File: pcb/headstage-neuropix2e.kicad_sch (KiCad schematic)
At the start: 7 parts, among them J1 X.FL-R-SMT-1(02)

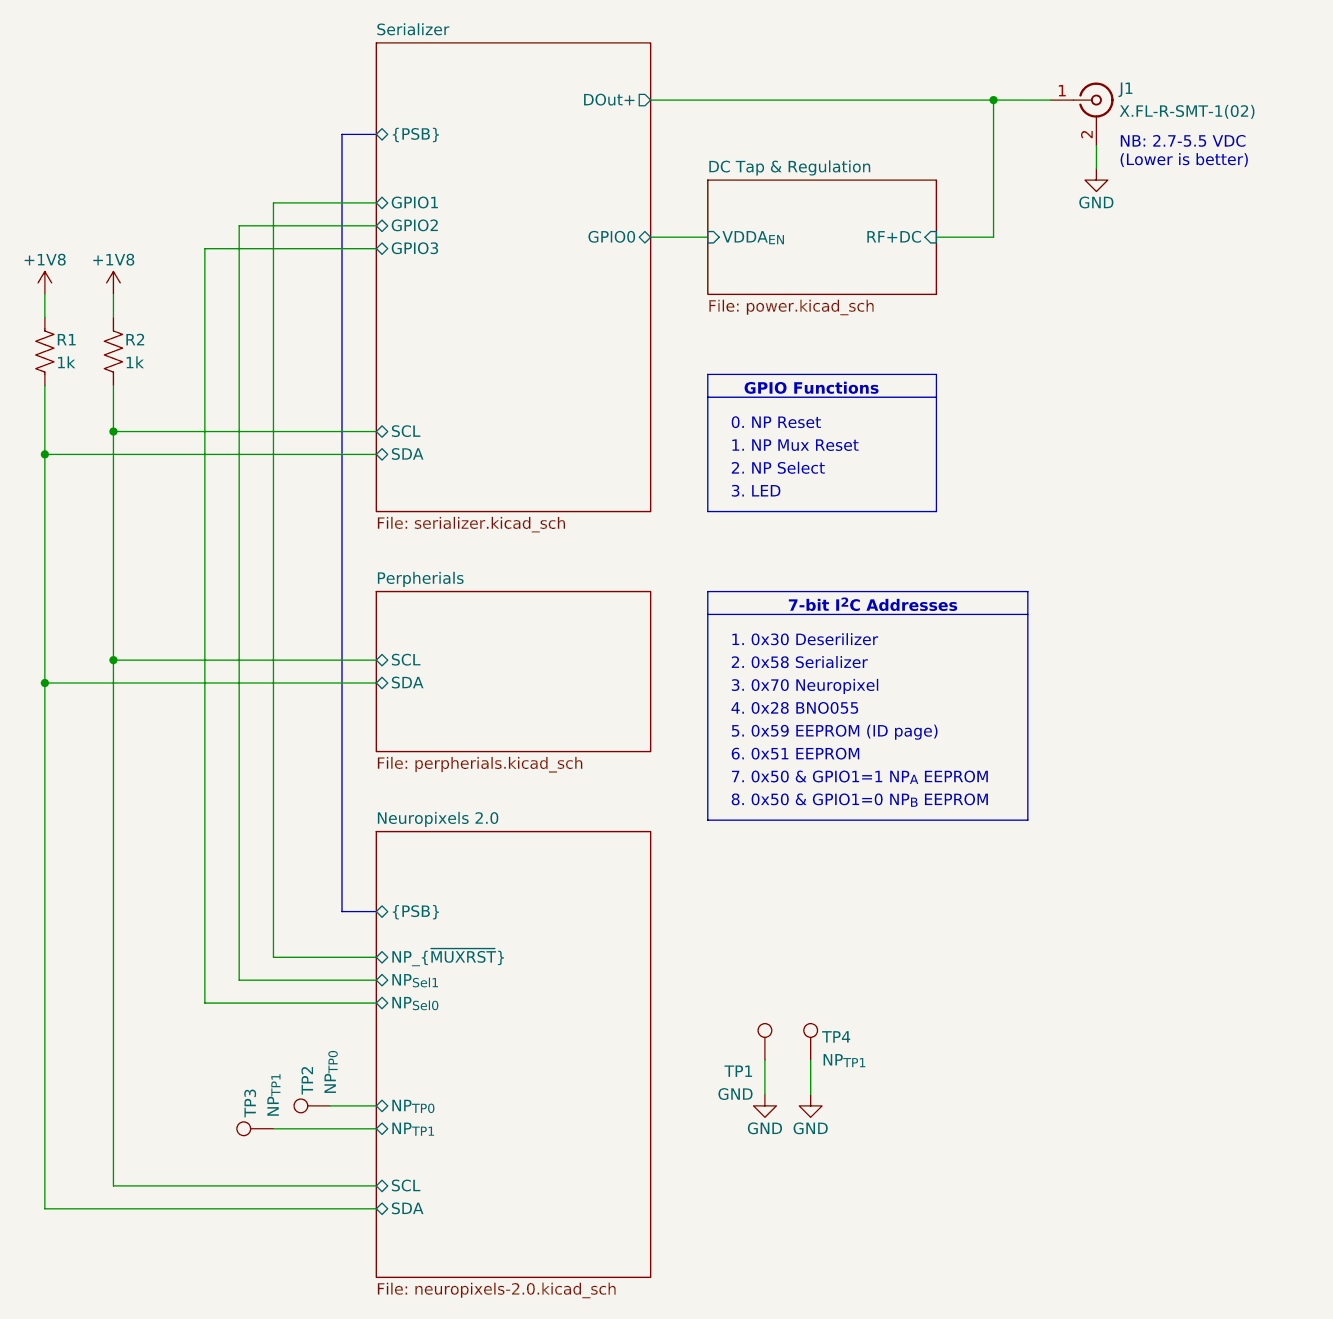
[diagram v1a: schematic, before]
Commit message: Revision B
- Fix incorrect STG3856 symbol and make corresponding changes to PCB
- Flip bits 1 and 2 in probe interaces (fixes #1)
- Improve silkscreen
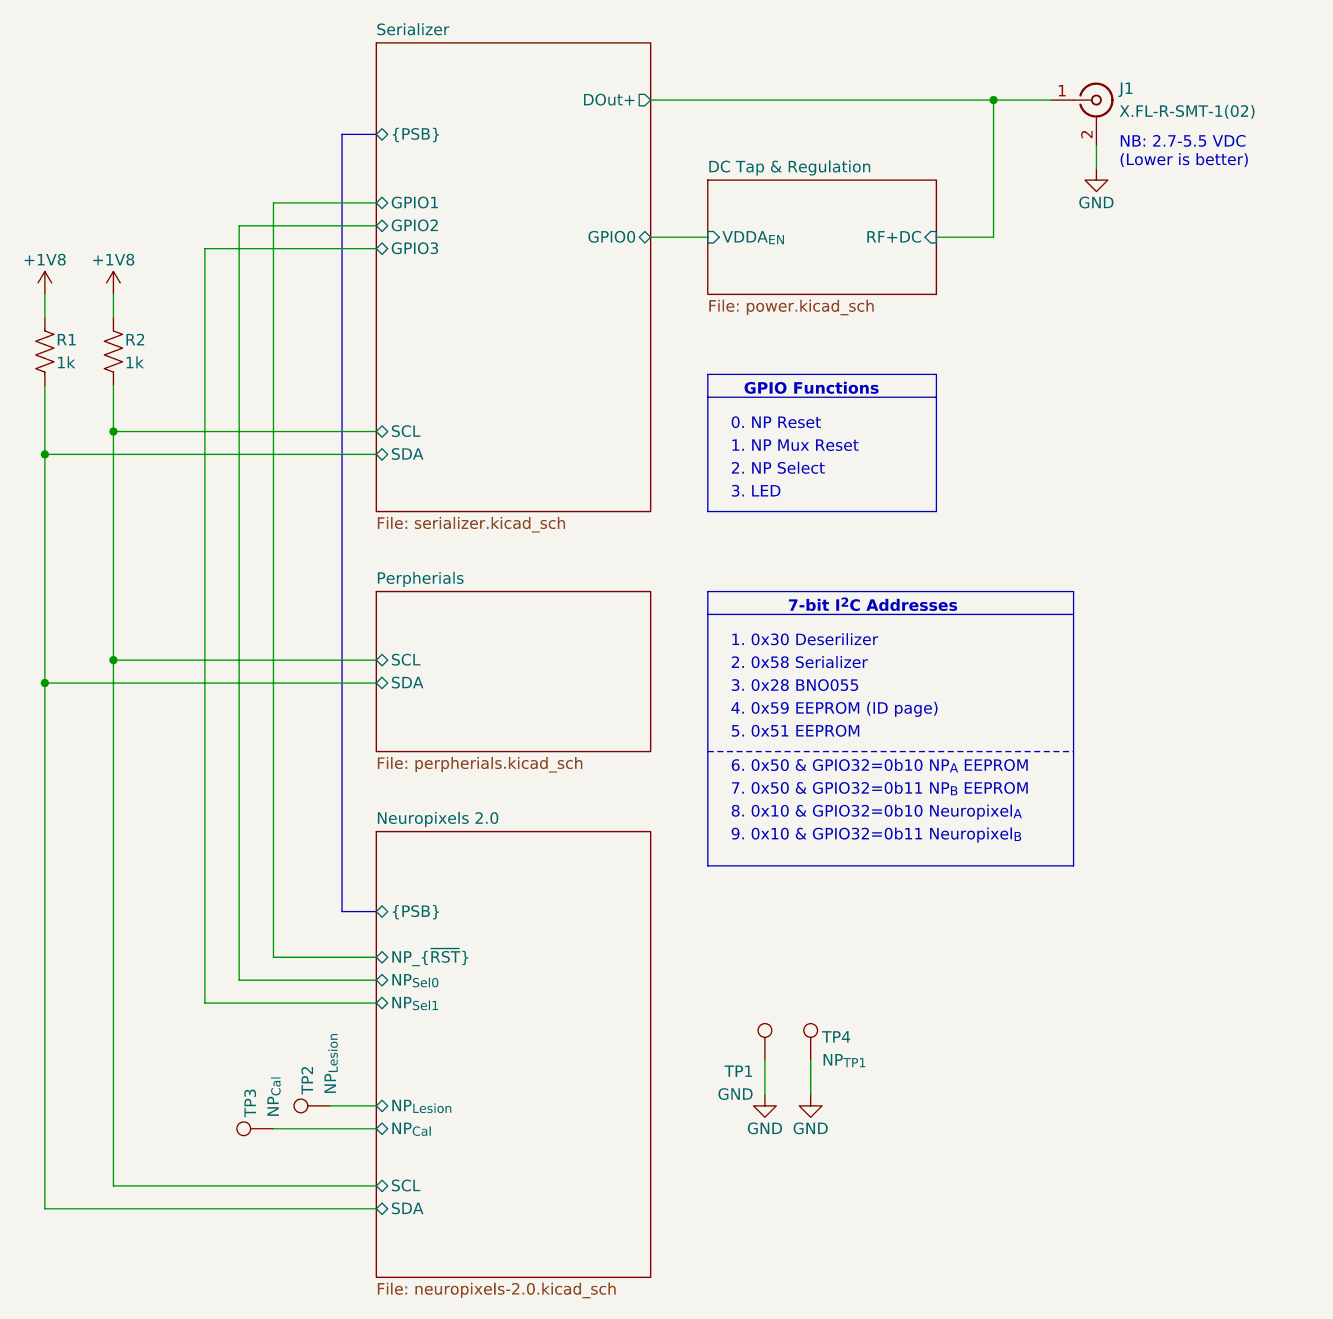
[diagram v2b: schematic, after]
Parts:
- J1, R1, R2, TP1, TP4: OEPS PN (none) -> ??
- TP2: value NP_{TP0} -> NP_{Lesion}; OEPS PN (none) -> ??
- TP3: value NP_{TP1} -> NP_{Cal}; OEPS PN (none) -> ??
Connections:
- net Neuropixels 2.0/NP_{TP0} renamed Neuropixels 2.0/NP_{Lesion}
- net Neuropixels 2.0/NP_{TP1} renamed Neuropixels 2.0/NP_{Cal}
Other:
- sheet Neuropixels 2.0 ports: added NP_{Cal}, NP_{Lesion}, NP_{~{RST}}; removed NP_{TP0}, NP_{TP1}, NP_{~{MUXRST}}
- note added: "3. 0x28 BNO055"
- note added: "4. 0x59 EEPROM (ID page)"
- note added: "5. 0x51 EEPROM"
- note added: "6. 0x50 & GPIO32=0b10 NP_{A} EEPROM"
- note added: "7. 0x50 & GPIO32=0b11 NP_{B} EEPROM"
- note added: "8. 0x10 & GPIO32=0b10 Neuropixel_{A}"
- note added: "9. 0x10 & GPIO32=0b11 Neuropixel_{B}"
- note removed: "3. 0x70 Neuropixel"
- note removed: "4. 0x28 BNO055"
- note removed: "5. 0x59 EEPROM (ID page)"
- note removed: "6. 0x51 EEPROM"
- note removed: "7. 0x50 & GPIO1=1 NP_{A} EEPROM"
- note removed: "8. 0x50 & GPIO1=0 NP_{B} EEPROM"
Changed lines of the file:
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@@
   (title_block
     (title "ONIX Neuropixels 2.0 Economical Headstage")
-    (rev "A")
+    (rev "B")
     (company "Open Ephys, Inc")
     (comment 1 "Jonathan P. Newman")
@@
     (stroke (width 0) (type default))
   )
-  (polyline (pts (xy 151.13 91.44) (xy 151.13 116.84))
+  (polyline (pts (xy 151.13 91.44) (xy 151.13 121.92))
     (stroke (width 0) (type default))
   )
@@
     (stroke (width 0) (type default))
   )
-  (polyline (pts (xy 151.13 93.98) (xy 186.69 93.98))
+  (polyline (pts (xy 151.13 93.98) (xy 191.77 93.98))
     (stroke (width 0) (type default))
   )
@@
     (stroke (width 0) (type default))
   )
-  (polyline (pts (xy 151.13 91.44) (xy 186.69 91.44))
+  (polyline (pts (xy 151.13 91.44) (xy 191.77 91.44))
     (stroke (width 0) (type default))
   )
@@
     (stroke (width 0) (type default))
   )
-  (polyline (pts (xy 186.69 91.44) (xy 186.69 116.84))
-    (stroke (width 0) (type default))
+  (polyline (pts (xy 191.77 91.44) (xy 191.77 121.92))
+    (stroke (width 0) (type default))
+  )
+  (polyline (pts (xy 151.13 109.22) (xy 191.77 109.22))
+    (stroke (width 0) (type dot))
   )
   (wire (pts (xy 77.47 68.58) (xy 77.47 76.2))
@@
     (stroke (width 0) (type default))
   )
-  (polyline (pts (xy 186.69 116.84) (xy 151.13 116.84))
+  (polyline (pts (xy 191.77 121.92) (xy 151.13 121.92))
     (stroke (width 0) (type default))
   )
@@
     (effects (font (size 1.27 1.27) (thickness 0.254) bold) (justify left bottom))
   )
-  (text "6. 0x51 EEPROM\n" (at 153.67 110.49 0)
+  (text "5. 0x51 EEPROM\n" (at 153.67 107.95 0)
     (effects (font (size 1.27 1.27)) (justify left bottom))
   )
@@
     (effects (font (size 1.27 1.27)) (justify left bottom))
   )
-  (text "8. 0x50 & GPIO1=0 NP_{B} EEPROM\n" (at 153.67 115.57 0)
-    (effects (font (size 1.27 1.27)) (justify left bottom))
-  )
-  (text "4. 0x28 BNO055\n" (at 153.67 105.41 0)
+  (text "7. 0x50 & GPIO32=0b11 NP_{B} EEPROM\n" (at 153.67 114.3 0)
+    (effects (font (size 1.27 1.27)) (justify left bottom))
+  )
+  (text "3. 0x28 BNO055\n" (at 153.67 102.87 0)
     (effects (font (size 1.27 1.27)) (justify left bottom))
   )
@@
     (effects (font (size 1.27 1.27)) (justify left bottom))
   )
-  (text "7. 0x50 & GPIO1=1 NP_{A} EEPROM\n" (at 153.67 113.03 0)
+  (text "6. 0x50 & GPIO32=0b10 NP_{A} EEPROM\n" (at 153.67 111.76 0)
     (effects (font (size 1.27 1.27)) (justify left bottom))
   )
@@
     (effects (font (size 1.27 1.27)) (justify left bottom))
   )
-  (text "5. 0x59 EEPROM (ID page)\n" (at 153.67 107.95 0)
+  (text "4. 0x59 EEPROM (ID page)\n" (at 153.67 105.41 0)
     (effects (font (size 1.27 1.27)) (justify left bottom))
   )
@@
     (effects (font (size 1.27 1.27)) (justify left bottom))
   )
-  (text "3. 0x70 Neuropixel\n" (at 153.67 102.87 0)
+  (text "9. 0x10 & GPIO32=0b11 Neuropixel_{B}\n" (at 153.67 119.38 0)
+    (effects (font (size 1.27 1.27)) (justify left bottom))
+  )
+  (text "8. 0x10 & GPIO32=0b10 Neuropixel_{A}\n" (at 153.67 116.84 0)
     (effects (font (size 1.27 1.27)) (justify left bottom))
   )
@@
       (effects (font (size 1.27 1.27)) (justify left))
     )
-    (property "Value" "NP_{TP1}" (at 102.87 149.86 0)
+    (property "Value" "NP_{Cal}" (at 102.87 149.86 0)
       (effects (font (size 1.27 1.27)) (justify left))
     )
@@
       (effects (font (size 1.27 1.27)) hide)
     )
+    (property "OEPS PN" "??" (at 102.87 151.13 0)
+      (effects (font (size 1.27 1.27)) hide)
+    )
     (pin "1")
     (instances
@@
     )
     (property "Tolerance" "1%" (at 77.47 64.77 0)
+      (effects (font (size 1.27 1.27)) hide)
+    )
+    (property "OEPS PN" "??" (at 77.47 64.77 0)
       (effects (font (size 1.27 1.27)) hide)
     )
@@
       (effects (font (size 1.27 1.27)) hide)
     )
+    (property "OEPS PN" "??" (at 85.09 64.77 0)
+      (effects (font (size 1.27 1.27)) hide)
+    )
     (pin "1")
     (pin "2")
@@
     )
     (property "Tolerance" "" (at 194.31 36.83 0)
+      (effects (font (size 1.27 1.27)) hide)
+    )
+    (property "OEPS PN" "??" (at 194.31 36.83 0)
       (effects (font (size 1.27 1.27)) hide)
     )
@@
       (effects (font (size 1.27 1.27)) hide)
     )
+    (property "OEPS PN" "??" (at 162.56 143.51 0)
+      (effects (font (size 1.27 1.27)) hide)
+    )
     (pin "1")
     (instances
@@
       (effects (font (size 1.27 1.27)) hide)
     )
+    (property "OEPS PN" "??" (at 157.48 143.51 0)
+      (effects (font (size 1.27 1.27)) hide)
+    )
     (pin "1")
     (instances
@@
       (effects (font (size 1.27 1.27)) (justify left))
     )
-    (property "Value" "NP_{TP0}" (at 109.22 147.32 0)
+    (property "Value" "NP_{Lesion}" (at 109.22 147.32 0)
       (effects (font (size 1.27 1.27)) (justify left))
     )
@@
     )
     (property "Tolerance" "" (at 109.22 148.59 0)
+      (effects (font (size 1.27 1.27)) hide)
+    )
+    (property "OEPS PN" "??" (at 109.22 148.59 0)
       (effects (font (size 1.27 1.27)) hide)
     )
@@
       (effects (font (size 1.27 1.27)) (justify left))
     )
-    (pin "NP_{TP0}" bidirectional (at 114.3 148.59 180)
+    (pin "NP_{Lesion}" bidirectional (at 114.3 148.59 180)
       (effects (font (size 1.27 1.27)) (justify left))
     )
@@
       (effects (font (size 1.27 1.27)) (justify left))
     )
-    (pin "NP_{TP1}" bidirectional (at 114.3 151.13 180)
-      (effects (font (size 1.27 1.27)) (justify left))
-    )
-    (pin "NP_{~{MUXRST}}" bidirectional (at 114.3 132.08 180)
-      (effects (font (size 1.27 1.27)) (justify left))
-    )
-    (pin "NP_{Sel1}" bidirectional (at 114.3 134.62 180)
-      (effects (font (size 1.27 1.27)) (justify left))
-    )
-    (pin "NP_{Sel0}" bidirectional (at 114.3 137.16 180)
-      (effects (font (size 1.27 1.27)) (justify left))
-    )
+    (pin "NP_{Cal}" bidirectional (at 114.3 151.13 180)
+      (effects (font (size 1.27 1.27)) (justify left))
+    )
+    (pin "NP_{~{RST}}" bidirectional (at 114.3 132.08 180)
+      (effects (font (size 1.27 1.27)) (justify left))
+    )
+    (pin "NP_{Sel1}" bidirectional (at 114.3 137.16 180)
+      (effects (font (size 1.27 1.27)) (justify left))
+    )
+    (pin "NP_{Sel0}" bidirectional (at 114.3 134.62 180)
+      (effects (font (size 1.27 1.27)) (justify left))
+    )

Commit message: Added new fields (OEPS PN, MPN, and Type) to all components.
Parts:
- J1: MPN (none) -> X.FL-R-SMT-1(02); OEPS PN ?? -> OEPS070052; Type (none) -> SMD
- R1, R2: MPN (none) -> RC0201FR-071KL; OEPS PN ?? -> OEPS020065; Type (none) -> SMD
- TP1, TP2, TP3, TP4: MPN (none) -> -; OEPS PN ?? -> -; Type (none) -> -
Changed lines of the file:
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@@
       (effects (font (size 1.27 1.27)) hide)
     )
-    (property "OEPS PN" "??" (at 102.87 151.13 0)
+    (property "OEPS PN" "-" (at 102.87 151.13 0)
+      (effects (font (size 1.27 1.27)) hide)
+    )
+    (property "MPN" "-" (at 102.87 151.13 0)
+      (effects (font (size 1.27 1.27)) hide)
+    )
+    (property "Type" "-" (at 102.87 151.13 0)
       (effects (font (size 1.27 1.27)) hide)
     )
@@
       (effects (font (size 1.27 1.27)) hide)
     )
-    (property "OEPS PN" "??" (at 77.47 64.77 0)
+    (property "OEPS PN" "OEPS020065" (at 77.47 64.77 0)
+      (effects (font (size 1.27 1.27)) hide)
+    )
+    (property "MPN" "RC0201FR-071KL" (at 77.47 64.77 0)
+      (effects (font (size 1.27 1.27)) hide)
+    )
+    (property "Type" "SMD" (at 77.47 64.77 0)
       (effects (font (size 1.27 1.27)) hide)
     )
@@
       (effects (font (size 1.27 1.27)) hide)
     )
-    (property "OEPS PN" "??" (at 85.09 64.77 0)
+    (property "OEPS PN" "OEPS020065" (at 85.09 64.77 0)
+      (effects (font (size 1.27 1.27)) hide)
+    )
+    (property "MPN" "RC0201FR-071KL" (at 85.09 64.77 0)
+      (effects (font (size 1.27 1.27)) hide)
+    )
+    (property "Type" "SMD" (at 85.09 64.77 0)
       (effects (font (size 1.27 1.27)) hide)
     )
@@
       (effects (font (size 1.27 1.27)) hide)
     )
-    (property "OEPS PN" "??" (at 194.31 36.83 0)
+    (property "OEPS PN" "OEPS070052" (at 194.31 36.83 0)
+      (effects (font (size 1.27 1.27)) hide)
+    )
+    (property "MPN" "X.FL-R-SMT-1(02)" (at 194.31 36.83 0)
+      (effects (font (size 1.27 1.27)) hide)
+    )
+    (property "Type" "SMD" (at 194.31 36.83 0)
       (effects (font (size 1.27 1.27)) hide)
     )
@@
       (effects (font (size 1.27 1.27)) hide)
     )
-    (property "OEPS PN" "??" (at 162.56 143.51 0)
+    (property "OEPS PN" "-" (at 162.56 143.51 0)
+      (effects (font (size 1.27 1.27)) hide)
+    )
+    (property "MPN" "-" (at 162.56 143.51 0)
+      (effects (font (size 1.27 1.27)) hide)
+    )
+    (property "Type" "-" (at 162.56 143.51 0)
       (effects (font (size 1.27 1.27)) hide)
     )
@@
       (effects (font (size 1.27 1.27)) hide)
     )
-    (property "OEPS PN" "??" (at 157.48 143.51 0)
+    (property "OEPS PN" "-" (at 157.48 143.51 0)
+      (effects (font (size 1.27 1.27)) hide)
+    )
+    (property "MPN" "-" (at 157.48 143.51 0)
+      (effects (font (size 1.27 1.27)) hide)
+    )
+    (property "Type" "-" (at 157.48 143.51 0)
       (effects (font (size 1.27 1.27)) hide)
     )
@@
       (effects (font (size 1.27 1.27)) hide)
     )
-    (property "OEPS PN" "??" (at 109.22 148.59 0)
-      (effects (font (size 1.27 1.27)) hide)
-    )
+    (property "OEPS PN" "-" (at 109.22 148.59 0)
+      (effects (font (size 1.27 1.27)) hide)
+    )
+    (property "MPN" "-" (at 109.22 148.59 0)
+      (effects (font (size 1.27 1.27)) hide)
+    )
+    (property "Type" "-" (at 109.22 148.59 0)
+      (effects (font (size 1.27 1.27)) hide)
+    )
